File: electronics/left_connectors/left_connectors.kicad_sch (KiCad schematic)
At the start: 13 parts, among them J1 USB_C_Receptacle_USB2.0, J2 Audio In, J3 Conn_01x18_Pin, SW1 Power, SW2 ANC_control

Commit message: schematic done, blocks located, uC1 + PWR routed
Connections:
- net ANC_OFF: now also J3.11 (Pin_11); no longer J3.7 (Pin_7)
- net ANC_ON: now also J3.12 (Pin_12); no longer J3.8 (Pin_8)
- net ANC_PBO: now also J3.10 (Pin_10); no longer J3.6 (Pin_6)
- net GNDA: now also J3.1 (Pin_1); no longer J3.12 (Pin_12)
- net LEDs_data_in: now also J3.9 (Pin_9); no longer J3.5 (Pin_5)
- net PWR_SW: now also J3.13 (Pin_13); no longer J3.9 (Pin_9)
- net USB_D+: now also J3.14 (Pin_14); no longer J3.10 (Pin_10)
- net USB_D-: now also J3.15 (Pin_15); no longer J3.11 (Pin_11)
- net audio_in_L: now also J3.2 (Pin_2); no longer J3.13 (Pin_13)
- net audio_in_R: now also J3.3 (Pin_3); no longer J3.14 (Pin_14)
- net audio_in_detect: now also J3.4 (Pin_4); no longer J3.15 (Pin_15)

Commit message: L filterers + drivers layout
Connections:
- net ANC_OFF: now also J3.13 (Pin_13); no longer J3.11 (Pin_11)
- net ANC_ON: now also J3.14 (Pin_14); no longer J3.12 (Pin_12)
- net ANC_PBO: now also J3.12 (Pin_12); no longer J3.10 (Pin_10)
- net LEDs_data_in: now also J3.11 (Pin_11); no longer J3.9 (Pin_9)
- net PWR_SW: now also J3.15 (Pin_15); no longer J3.13 (Pin_13)
- net USB_D+: now also J3.9 (Pin_9); no longer J3.14 (Pin_14)
- net USB_D-: now also J3.10 (Pin_10); no longer J3.15 (Pin_15)

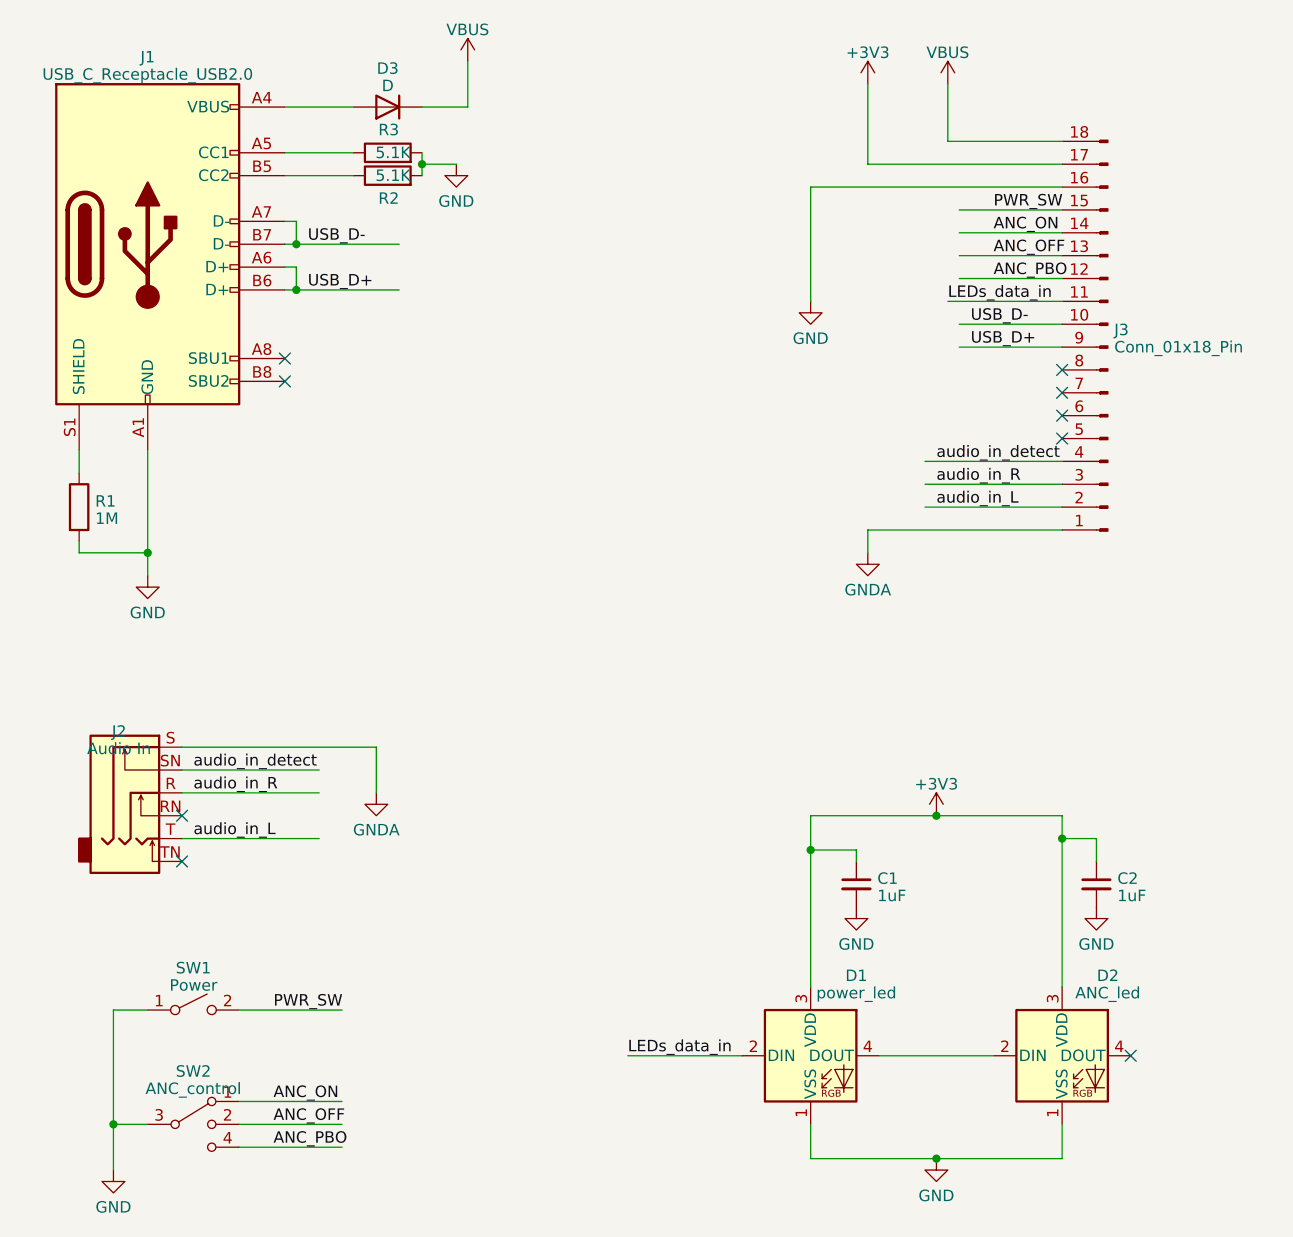
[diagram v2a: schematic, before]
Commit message: connectors board parts allocated
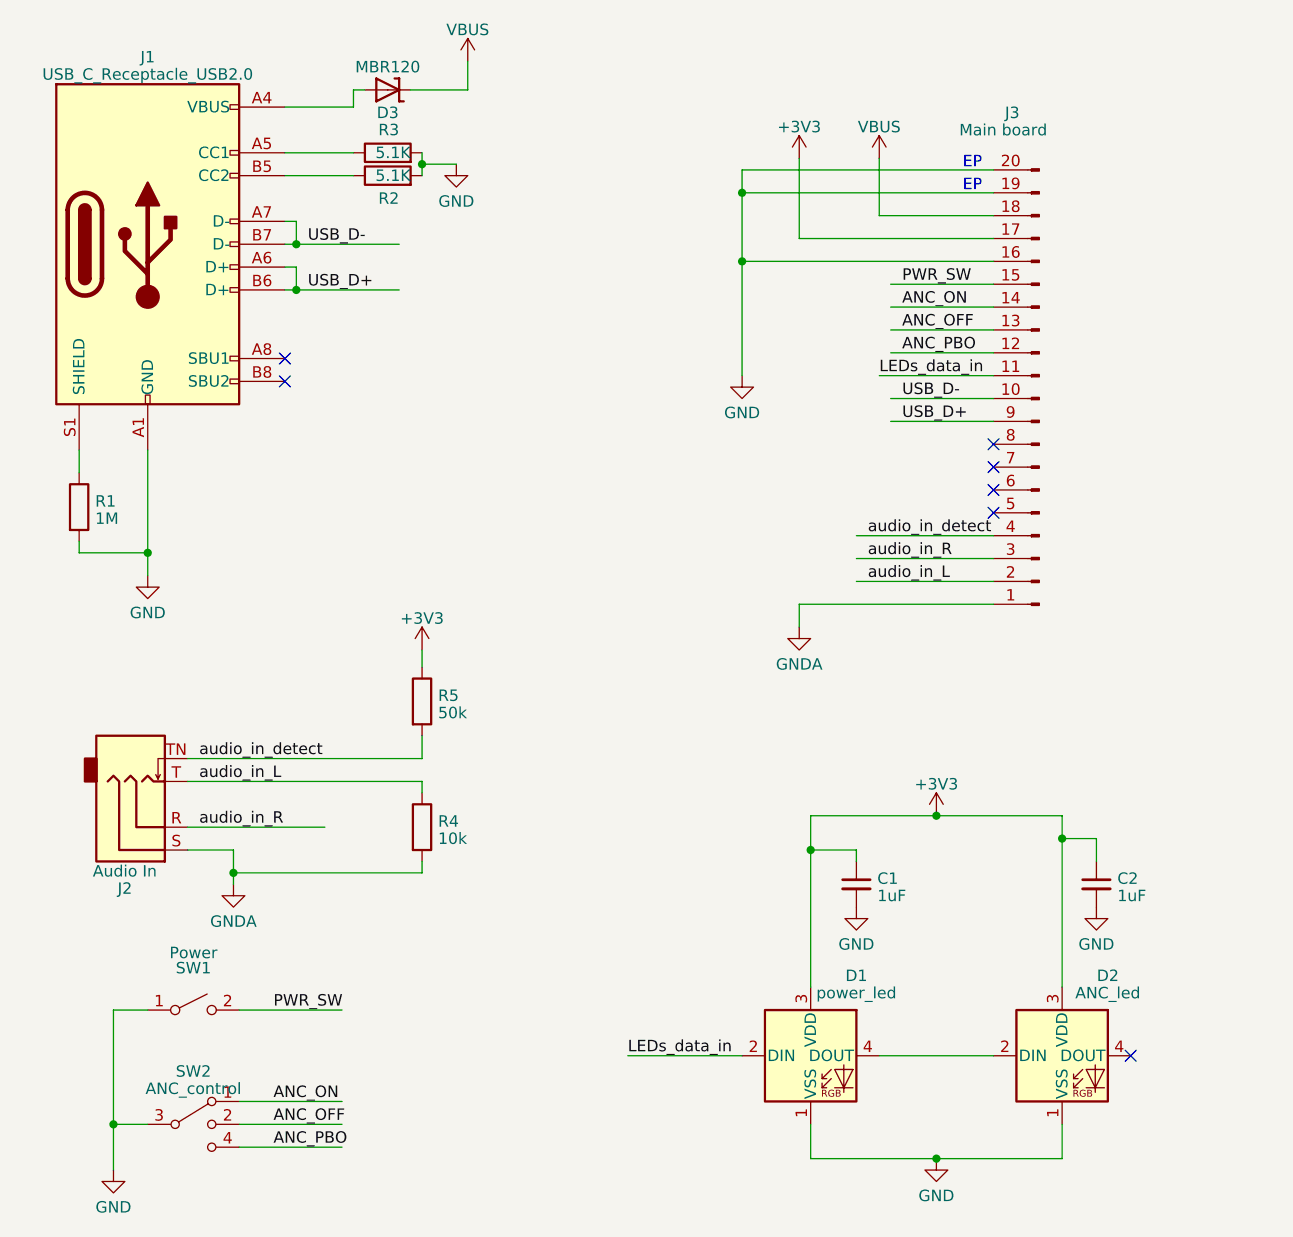
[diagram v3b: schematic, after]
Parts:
- removed D3: D, symbol Device:D
- removed J3: Conn_01x18_Pin, symbol Connector:Conn_01x18_Pin
- added D3: MBR120, Diode_SMD:D_SOD-123, symbol Adafruit Feather M0 Basic rev C-eagle-import:DIODE-SCHOTTKYSOD-123
- added J3: Main board, FH12-18S-0.5SVA(54):CON18_1X18_DUTB_HRS_HIR, symbol Connector:Conn_01x20_Pin
- added R4: 10k, Resistor_SMD:R_0402_1005Metric_Pad0.72x0.64mm_HandSolder, symbol Device:R
- added R5: 50k, Resistor_SMD:R_0402_1005Metric_Pad0.72x0.64mm_HandSolder, symbol Device:R
- C1, C2: footprint (none) -> Capacitor_SMD:C_0402_1005Metric_Pad0.74x0.62mm_HandSolder
- D1, D2: footprint LED_SMD:LED_SK6812_PLCC4_5.0x5.0mm_P3.2mm -> LED_SMD:LED_SK6812_EC15_1.5x1.5mm
- J1: footprint (none) -> USB4110-GF-A_REVB:GCT_USB4110-GF-A_REVB
- J2: footprint (none) -> SJ-3524-SMT:CUI_SJ-3524-SMT; symbol Connector_Audio:AudioJack3_Switch -> Connector_Audio:AudioJack3_SwitchT
- R1, R2, R3: footprint (none) -> Resistor_SMD:R_0402_1005Metric_Pad0.72x0.64mm_HandSolder
- SW1: footprint (none) -> ul_EVQ-P7A01P:EVQ_P7_PAN
- SW2: footprint (none) -> CUS-13TB:CUS13B
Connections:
- net +3V3: now also J3.17 (Pin_17), R5.1
- net ANC_OFF: now also J3.13 (Pin_13)
- net ANC_ON: now also J3.14 (Pin_14)
- net ANC_PBO: now also J3.12 (Pin_12)
- net GND: now also J3.16 (Pin_16), J3.19 (Pin_19), J3.20 (Pin_20)
- net GNDA: now also J3.1 (Pin_1), R4.2
- net LEDs_data_in: now also J3.11 (Pin_11)
- net PWR_SW: now also J3.15 (Pin_15)
- net USB_D+: now also J3.9 (Pin_9)
- net USB_D-: now also J3.10 (Pin_10)
- net VBUS: now also D3.1 (C), J3.18 (Pin_18)
- net audio_in_L: now also J3.2 (Pin_2), R4.1
- net audio_in_R: now also J3.3 (Pin_3)
- net audio_in_detect: now also J2.TN, J3.4 (Pin_4), R5.2; no longer J2.SN
- net at J1.A4 (VBUS), J1.A9 (VBUS), J1.B4 (VBUS)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: now also D3.2 (A)
- no-connect marks 9 -> 7
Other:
- note added: "EP"

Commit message: pcbs done, filters need to be finalised
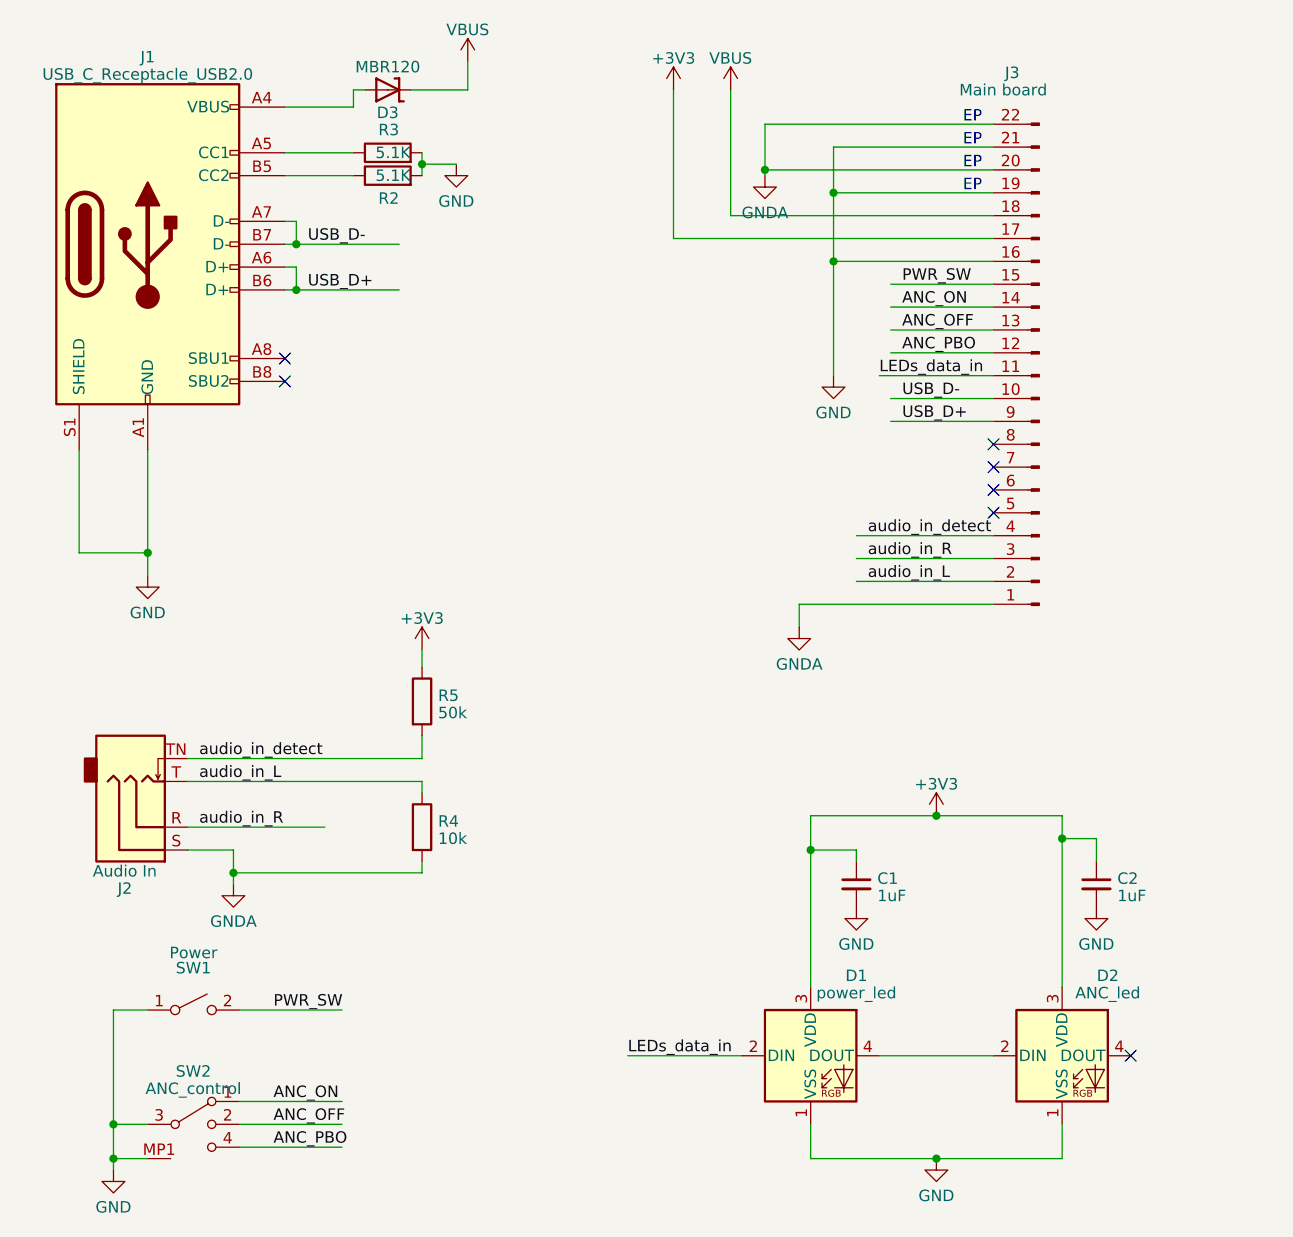
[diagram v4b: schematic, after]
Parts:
- removed R1: 1M, Resistor_SMD:R_0402_1005Metric_Pad0.72x0.64mm_HandSolder, symbol Device:R
- J2: footprint SJ-3524-SMT:CUI_SJ-3524-SMT -> SCHURTER Inc 4832.2330:4832.2330
- J3: symbol Connector:Conn_01x20_Pin -> Connector:Conn_01x22_Pin
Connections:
- net GND: now also J1.S1 (SHIELD), J3.21 (Pin_21), SW2.MP1, SW2.MP2, SW2.MP3, SW2.MP4; no longer J3.20 (Pin_20)
- net GNDA: now also J3.20 (Pin_20), J3.22 (Pin_22)
